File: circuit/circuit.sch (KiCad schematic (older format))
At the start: 19 parts

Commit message: circuit building
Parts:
- added BATT1, BATT2, BATT3, BATT4: M02PTH, SparkFun:SparkFun-1X02_XTRA_BIG, symbol M02PTH
- added C-ADC1: 100n, Capacitors_SMD:C_0805_HandSoldering, symbol C
- added CON-PV1: BARREL_JACK, Connect:JACK_ALIM, symbol BARREL_JACK
- added C_VUSB1, C_VUSB2: 100u, Capacitors_ThroughHole:C_Radial_D5_L6_P2.5, symbol CP
- added D-3V3, D-LAMP1, D-PV1, D-USB1, D-VDD1: D, Diodes_SMD:SMA_Handsoldering, symbol D
- added D-VUSB1, D-VUSB2: D_Schottky, Diodes_SMD:SMA_Handsoldering, symbol D_Schottky
- added D1: 5v1, Diodes_SMD:MELF_Handsoldering, symbol ZENER
- added IC-VUSB1: LM2596S, TO_SOT_Packages_SMD:TO-263-5Lead, symbol LM2596S
- added L-VUSB1: INDUCTOR, Inductors:INDUCTOR_V, symbol INDUCTOR
- added OK-LAMP1, OK-PV1, OK-PV2, OK-USB1: PC817, Housings_DIP:DIP-4_W7.62mm, symbol PC817
- added P-VDD-3V3, SW-PWR1: CONN_01X02, Pin_Headers:Pin_Header_Straight_1x02, symbol CONN_01X02
- added P1: USB_A, Connect:USB_A, symbol USB_A
- added R-ADC-BATT1: 470k, Resistors_ThroughHole:Resistor_Horizontal_RM10mm, symbol R
- added R-ADC-BATT2: 100k, Resistors_ThroughHole:Resistor_Horizontal_RM10mm, symbol R
- added R-LAMP1, R-PV3, R-USB1: 330, Resistors_SMD:R_0805_HandSoldering, symbol R
- added R-LAMP2, R-PV1, R-PV4, R-USB2: 4k7, Resistors_SMD:R_0805_HandSoldering, symbol R
- added R-PV2: 100k, Resistors_SMD:R_0805_HandSoldering, symbol R
- added TR-LAMP1, TR-USB1: IRF530_TO220BV, transistor-power:TO220BV, symbol IRF530_TO220BV
- added TR-PV1: IRF9530_TO220BV, transistor-power:TO220BV, symbol IRF9530_TO220BV
- added U1: MIC5219BM5_SOT23-5, TO_SOT_Packages_SMD:SOT-23-5, symbol MIC5219BM5_SOT23-5
- L-LAMP1, L-PV1, L-USB1, L1, L2, L3, L4: footprint LEDs:LED-1206 -> LEDs:LED-0805
- R-L-LAMP1, R-L-PV1, R-L-USB1, R-L1, R-L2, R-L3, R-L4, R-NRST1: footprint Resistors_SMD:R_1206_HandSoldering -> Resistors_SMD:R_0805_HandSoldering
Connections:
- net +3V3: now also D-3V3.1 (K), P-VDD-3V3.2 (P2)
- net ADC_BATT: now also C-ADC1.1, R-ADC-BATT1.2, R-ADC-BATT2.1
- net ADC_USB: now also D-VUSB2.2 (A), P1.4 (GND), P1.5 (shield)
- net GND: now also C-ADC1.2, C_VUSB1.2, C_VUSB2.2, D-VUSB1.2 (A), D-VUSB2.1 (K), D1.2 (A), IC-VUSB1.3 (GND), IC-VUSB1.5 (EN), IC-VUSB1.6 (GND@1), OK-LAMP1.2, OK-PV1.2, OK-PV2.2, OK-USB1.2, R-ADC-BATT2.2, R-LAMP2.2, R-PV1.2, R-USB2.2, SW-PWR1.1 (P1), U1.2 (GND)
- net RX: now also P-COMM1.3 (P3); no longer P-COMM1.4 (P4)
- net TX: now also P-COMM1.4 (P4); no longer P-COMM1.3 (P3)
- net VDD: now also D-VDD1.1 (K), OK-PV1.4, P-VDD-3V3.1 (P1)
- net CON_PV: now reaches STM32.25 (PB12/TIM1_BKIN)
- net CON_PV: now also R-PV3.1
- net CON_LAMP: now reaches STM32.26 (PB13/TIM1_CH1N)
- net CON_LAMP: now also R-LAMP1.1
- net CON_USB: now reaches STM32.27 (PB14/TIM1_CH2N)
- net CON_USB: now also R-USB1.1
- net ADC_PV_WKUP renamed IND_PV_WKUP
- net IND_PV_WKUP: now also OK-PV1.3, R-PV1.1
- new net: BATT1.1, BATT2.2
- new net: BATT3.1, BATT4.2, D-VDD1.2 (A)
- new net: OK-PV1.1, R-PV2.2
- new net: D-3V3.2 (A), U1.5 (OUT)
- new net: OK-PV2.1, R-PV3.2
- new net: OK-PV2.3, R-PV4.1, TR-PV1.G
- new net: D-PV1.2 (A), TR-PV1.D
- new net: OK-LAMP1.1, R-LAMP1.2
- new net: OK-LAMP1.3, R-LAMP2.1, TR-LAMP1.G
- new net: D-LAMP1.1 (K), OK-LAMP1.4, TR-LAMP1.D
- new net: C_VUSB1.1, IC-VUSB1.1 (IN), TR-USB1.S
- new net: D-VUSB1.1 (K), IC-VUSB1.2 (OUT), L-VUSB1.2
- new net: C_VUSB2.1, D1.1 (K), IC-VUSB1.4 (FB), L-VUSB1.1, P1.1 (VCC)
- new net: OK-USB1.1, R-USB1.2
- new net: OK-USB1.3, R-USB2.1, TR-USB1.G
- new net: D-USB1.1 (K), OK-USB1.4, TR-USB1.D
- new net +15V: BATT1.2, D-LAMP1.2 (A), D-PV1.1 (K), D-USB1.2 (A), R-ADC-BATT1.1
- new net +24V: CON-PV1.1, OK-PV2.4, R-PV2.1, TR-PV1.S
- new net +6V: BATT2.1, BATT3.2, U1.1 (IN), U1.3 (EN)
- new net GNDPWR: BATT4.1, CON-PV1.2, CON-PV1.3, R-PV4.2, SW-PWR1.2 (P2)
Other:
- moved on the sheet: L-LAMP1, L-PV1, L-USB1, L1, L2, L3, L4, P-BOOT1, P-COMM1, R-L-LAMP1, R-L-PV1, R-L-USB1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

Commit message: development
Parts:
- added L-IND1: LED, LEDs:LED-0805, symbol LED
- added R-L-IND1: 330, Resistors_SMD:R_0805_HandSoldering, symbol R
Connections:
- net GND: now also L-IND1.1 (K)
- net L-IND: now reaches STM32.38 (JTDI/PA15)
- net L-IND: now also R-L-IND1.2
- new net: L-IND1.2 (A), R-L-IND1.1
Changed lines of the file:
@@
 $EndComp
 $Comp
-L GND #PWR30
+L GND #PWR31
 U 1 1 572719C0
 P 10350 3550
-F 0 "#PWR30" H 10350 3300 50  0001 C CNN
+F 0 "#PWR31" H 10350 3300 50  0001 C CNN
 F 1 "GND" H 10350 3400 50  0000 C CNN
 F 2 "" H 10350 3550 50  0000 C CNN
@@
 $EndComp
 $Comp
-L VDD #PWR28
+L VDD #PWR29
 U 1 1 572734AE
 P 9750 3150
-F 0 "#PWR28" H 9750 3000 50  0001 C CNN
+F 0 "#PWR29" H 9750 3000 50  0001 C CNN
 F 1 "VDD" H 9750 3300 50  0000 C CNN
 F 2 "" H 9750 3150 50  0000 C CNN
@@
 $EndComp
 $Comp
-L GND #PWR24
+L GND #PWR25
 U 1 1 572742F8
 P 9650 3850
-F 0 "#PWR24" H 9650 3600 50  0001 C CNN
+F 0 "#PWR25" H 9650 3600 50  0001 C CNN
 F 1 "GND" H 9650 3700 50  0000 C CNN
 F 2 "" H 9650 3850 50  0000 C CNN
@@
 IND_PV_WKUP
 $Comp
-L GNDPWR #PWR34
+L GNDPWR #PWR35
 U 1 1 57276075
 P 10700 2900
-F 0 "#PWR34" H 10700 2700 50  0001 C CNN
+F 0 "#PWR35" H 10700 2700 50  0001 C CNN
 F 1 "GNDPWR" H 10700 2770 50  0000 C CNN
 F 2 "" H 10700 2850 50  0000 C CNN
@@
 $EndComp
 $Comp
-L +24V #PWR29
+L +24V #PWR30
 U 1 1 572762B3
 P 10200 2850
-F 0 "#PWR29" H 10200 2700 50  0001 C CNN
+F 0 "#PWR30" H 10200 2700 50  0001 C CNN
 F 1 "+24V" H 10200 2990 50  0000 C CNN
 F 2 "" H 10200 2850 50  0000 C CNN
@@
 $EndComp
 $Comp
-L +24V #PWR36
+L +24V #PWR37
 U 1 1 5727D109
 P 10800 4250
-F 0 "#PWR36" H 10800 4100 50  0001 C CNN
+F 0 "#PWR37" H 10800 4100 50  0001 C CNN
 F 1 "+24V" H 10800 4390 50  0000 C CNN
 F 2 "" H 10800 4250 50  0000 C CNN
@@
 $EndComp
 $Comp
-L GND #PWR25
+L GND #PWR26
 U 1 1 5727D72F
 P 9650 4700
-F 0 "#PWR25" H 9650 4450 50  0001 C CNN
+F 0 "#PWR26" H 9650 4450 50  0001 C CNN
 F 1 "GND" H 9650 4550 50  0000 C CNN
 F 2 "" H 9650 4700 50  0000 C CNN
@@
 $EndComp
 $Comp
-L GNDPWR #PWR31
+L GNDPWR #PWR32
 U 1 1 5727E52D
 P 10450 5100
-F 0 "#PWR31" H 10450 4900 50  0001 C CNN
+F 0 "#PWR32" H 10450 4900 50  0001 C CNN
 F 1 "GNDPWR" H 10450 4970 50  0000 C CNN
 F 2 "" H 10450 5050 50  0000 C CNN
@@
 $EndComp
 $Comp
-L +15V #PWR38
+L +15V #PWR39
 U 1 1 5727EAFC
 P 11100 4800
-F 0 "#PWR38" H 11100 4650 50  0001 C CNN
+F 0 "#PWR39" H 11100 4650 50  0001 C CNN
 F 1 "+15V" H 11100 4940 50  0000 C CNN
 F 2 "" H 11100 4800 50  0000 C CNN
@@
 $EndComp
 $Comp
-L +15V #PWR37
+L +15V #PWR38
 U 1 1 57283181
 P 10850 5400
-F 0 "#PWR37" H 10850 5250 50  0001 C CNN
+F 0 "#PWR38" H 10850 5250 50  0001 C CNN
 F 1 "+15V" H 10850 5540 50  0000 C CNN
 F 2 "" H 10850 5400 50  0000 C CNN
@@
 $EndComp
 $Comp
-L GND #PWR26
+L GND #PWR27
 U 1 1 57283C11
 P 9650 6200
-F 0 "#PWR26" H 9650 5950 50  0001 C CNN
+F 0 "#PWR27" H 9650 5950 50  0001 C CNN
 F 1 "GND" H 9650 6050 50  0000 C CNN
 F 2 "" H 9650 6200 50  0000 C CNN
@@
 Connection ~ 10500 6200
 $Comp
-L GND #PWR33
+L GND #PWR34
 U 1 1 57289B95
 P 10500 6600
-F 0 "#PWR33" H 10500 6350 50  0001 C CNN
+F 0 "#PWR34" H 10500 6350 50  0001 C CNN
 F 1 "GND" H 10500 6450 50  0000 C CNN
 F 2 "" H 10500 6600 50  0000 C CNN
@@
 Connection ~ 10750 7550
 $Comp
-L +15V #PWR35
+L +15V #PWR36
 U 1 1 5728C61B
 P 10750 7000
-F 0 "#PWR35" H 10750 6850 50  0001 C CNN
+F 0 "#PWR36" H 10750 6850 50  0001 C CNN
 F 1 "+15V" H 10750 7140 50  0000 C CNN
 F 2 "" H 10750 7000 50  0000 C CNN
@@
 	10750 7000 10750 7150
 $Comp
-L GND #PWR27
+L GND #PWR28
 U 1 1 5728DC8C
 P 9650 7950
-F 0 "#PWR27" H 9650 7700 50  0001 C CNN
+F 0 "#PWR28" H 9650 7700 50  0001 C CNN
 F 1 "GND" H 9650 7800 50  0000 C CNN
 F 2 "" H 9650 7950 50  0000 C CNN
@@
 	9650 7900 9650 7950
 $Comp
-L GND #PWR32
+L GND #PWR33
 U 1 1 5728F192
 P 10450 8350
-F 0 "#PWR32" H 10450 8100 50  0001 C CNN
+F 0 "#PWR33" H 10450 8100 50  0001 C CNN
 F 1 "GND" H 10450 8200 50  0000 C CNN
 F 2 "" H 10450 8350 50  0000 C CNN
@@
 U 1 1 57274EE9
 P 6700 8250
-F 0 "U1" H 6700 8250 0   0001 C CNN
-F 1 "MIC5219BM5_SOT23-5" H 6700 8250 0   0001 C CNN
+F 0 "U1" H 6700 8250 60  0001 C CNN
+F 1 "MIC5219BM5_SOT23-5" H 6700 8250 60  0001 C CNN
 F 2 "TO_SOT_Packages_SMD:SOT-23-5" H 6700 8250 60  0001 C CNN
 F 3 "" H 6700 8250 60  0000 C CNN
@@
 	10950 8200 10750 8200
 $Comp
-L GND #PWR39
+L GND #PWR40
 U 1 1 57283CF9
 P 11200 8700
-F 0 "#PWR39" H 11200 8450 50  0001 C CNN
+F 0 "#PWR40" H 11200 8450 50  0001 C CNN
 F 1 "GND" H 11200 8550 50  0000 C CNN
 F 2 "" H 11200 8700 50  0000 C CNN
@@
 Wire Wire Line
 	10750 8200 10750 8000
+Wire Wire Line
+	6900 4500 7150 4500
+Text Label 7150 4500 0    60   ~ 0
+L-IND
+$Comp
+L R R-L-IND1
+U 1 1 57284423
+P 8300 6350
+F 0 "R-L-IND1" V 8380 6350 50  0000 C CNN
+F 1 "330" V 8300 6350 50  0000 C CNN
+F 2 "Resistors_SMD:R_0805_HandSoldering" V 8230 6350 50  0001 C CNN
+F 3 "" H 8300 6350 50  0000 C CNN
+	1    8300 6350
+	0    1    1    0
+$EndComp
+$Comp
+L LED L-IND1
+U 1 1 57284429
+P 8750 6350
+F 0 "L-IND1" H 8750 6450 50  0000 C CNN
+F 1 "LED" H 8750 6250 50  0000 C CNN
+F 2 "LEDs:LED-0805" H 8750 6350 50  0001 C CNN
+F 3 "" H 8750 6350 50  0000 C CNN
+	1    8750 6350
+	-1   0    0    1
+$EndComp
+Text Label 8050 6350 0    60   ~ 0
+L-IND
+$Comp
+L GND #PWR24
+U 1 1 57284430
+P 8950 6450
+F 0 "#PWR24" H 8950 6200 50  0001 C CNN
+F 1 "GND" H 8950 6300 50  0000 C CNN
+F 2 "" H 8950 6450 50  0000 C CNN
+F 3 "" H 8950 6450 50  0000 C CNN
+	1    8950 6450
+	1    0    0    -1
+$EndComp
+Wire Wire Line
+	8550 6350 8450 6350
+Wire Wire Line
+	8150 6350 8050 6350
+Wire Wire Line
+	8950 6350 8950 6450
 $EndSCHEMATC

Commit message: circuit building
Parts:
- added C-VREG1, C-VREG2: C, Capacitors_SMD:C_0805_HandSoldering, symbol C
- added D-LAMP2: D, Diodes_SMD:SMA_Handsoldering, symbol D
- added D-LAMP3: D_Schottky, Diodes_SMD:SMA_Handsoldering, symbol D_Schottky
- added J1: audio-jack, audio-lamp:JACK_LAPAN, symbol audio-jack
- added P2: CONN_01X04, Pin_Headers:Pin_Header_Straight_1x04, symbol CONN_01X04
- added PIN1: CONN_01X03, Pin_Headers:Pin_Header_Straight_1x03, symbol CONN_01X03
- added PIN2: CONN_01X06, Pin_Headers:Pin_Header_Straight_1x06, symbol CONN_01X06
- added PIN3: CONN_01X02, Pin_Headers:Pin_Header_Straight_1x02, symbol CONN_01X02
- U1: symbol MIC5219BM5_SOT23-5 -> MIC5219BM5_SOT23-5-RESCUE-circuit
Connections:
- net ADC_LAMP: now also D-LAMP3.2 (A), J1.1 (V-)
- net BOOT0: now also P-BOOT1.2 (P2); no longer P-BOOT1.1 (P1)
- net GND: now also C-VREG1.2, C-VREG2.2, D-LAMP3.1 (K)
- net VDD: now also P-BOOT1.1 (P1), STM32.1 (VBAT); no longer P-BOOT1.2 (P2)
- net AIN4: now reaches STM32.14 (SPI1_NSS/ADC1_IN4/USART2_CK/DAC1_OUT/PA4)
- net AIN4: now also PIN2.1 (P1)
- net AIN5: now reaches STM32.15 (SPI1_SCK/ADC1_IN5/DAC2_OUT/PA5)
- net AIN5: now also PIN2.2 (P2)
- net AIN6: now reaches STM32.16 (SPI1_MISO/ADC1_IN6/TIM3_CH1/PA6)
- net AIN6: now also PIN2.3 (P3)
- net AIN7: now reaches STM32.17 (SPI1_MOSI/ADC1_IN7/TIM3_CH2/PA7)
- net AIN7: now also PIN2.4 (P4)
- net AIN8: now reaches STM32.18 (PB0/ADC1_IN8/TIM3_CH3)
- net AIN8: now also PIN2.5 (P5)
- net AIN9: now reaches STM32.19 (PB1/ADC1_IN9/TIM3_CH4)
- net AIN9: now also PIN2.6 (P6)
- net PC13: now reaches STM32.2 (PC13/TAMPER_RTC)
- net PC13: now also PIN1.1 (P1)
- net PB15: now reaches STM32.28 (PB15/TIM1_CH3N/TIM15_CH1N)
- net PB15: now also PIN3.1 (P1)
- net PA8: now reaches STM32.29 (USART1_CK/MCO/TIM1_CH1/PA8)
- net PA8: now also PIN3.2 (P2)
- net PC14: now reaches STM32.3 (PC14/OSC32_IN)
- net PC14: now also PIN1.2 (P2)
- net PA11: now reaches STM32.32 (USART1_CTS/TIM1_CH4/PA11)
- net PA11: now also P2.1 (P1)
- net PA12: now reaches STM32.33 (USART1_RTS/TIM1_ETR/PA12)
- net PA12: now also P2.2 (P2)
- net PA13: now reaches STM32.34 (JTMS/SWDIO/PA13)
- net PA13: now also P2.3 (P3)
- net PA14: now reaches STM32.37 (JTCK/SWCLK/PA14)
- net PA14: now also P2.4 (P4)
- net PC15: now reaches STM32.4 (PC15/OSC32_OUT)
- net PC15: now also PIN1.3 (P3)
- net at U1.4 (BYP): now also C-VREG1.1
- net at D-3V3.2 (A), U1.5 (OUT): now also C-VREG2.1
- net at TR-LAMP1.S: now also D-LAMP2.2 (A)
- new net: D-LAMP2.1 (K), J1.2 (V+)

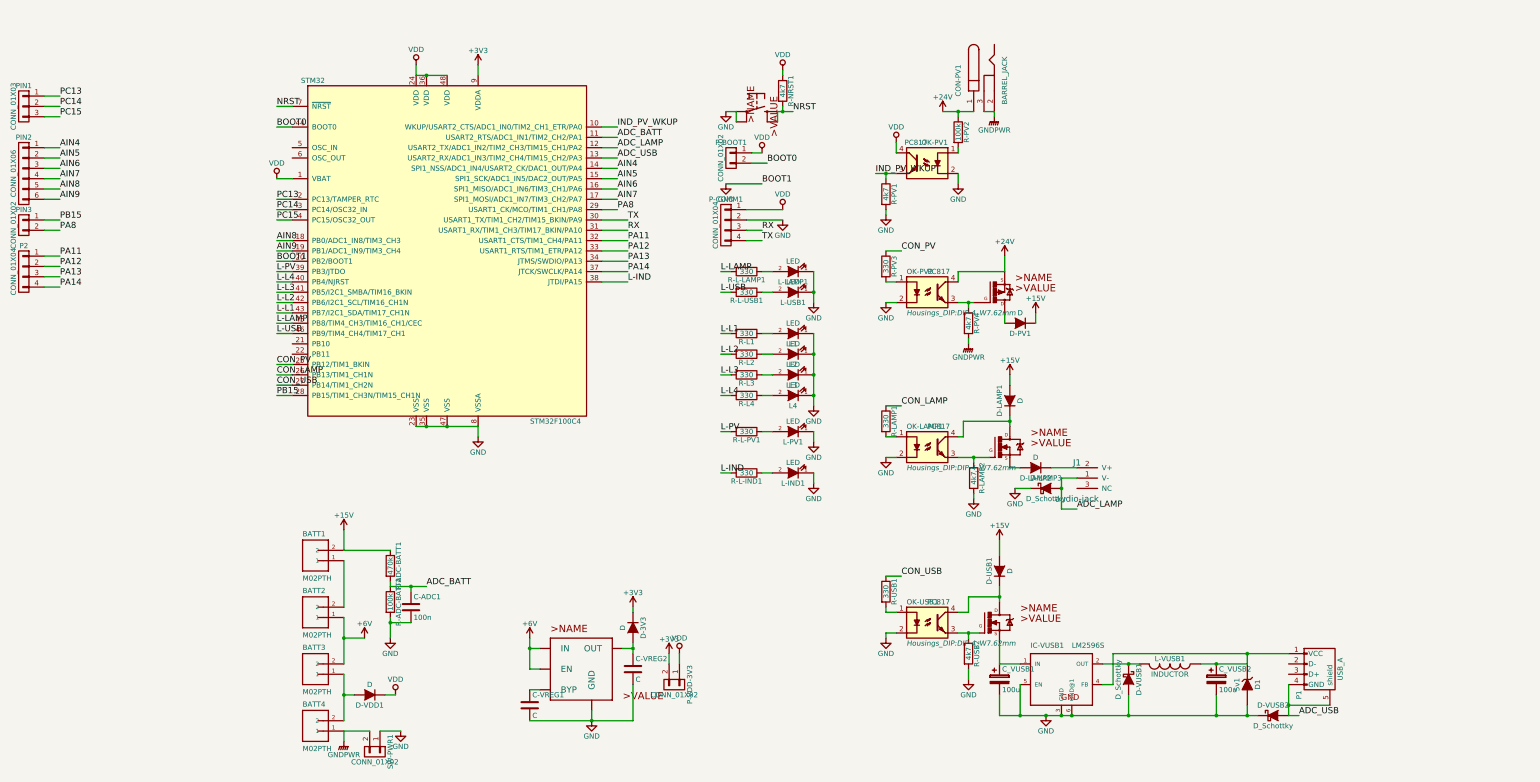
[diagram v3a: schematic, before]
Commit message: tambah test pad
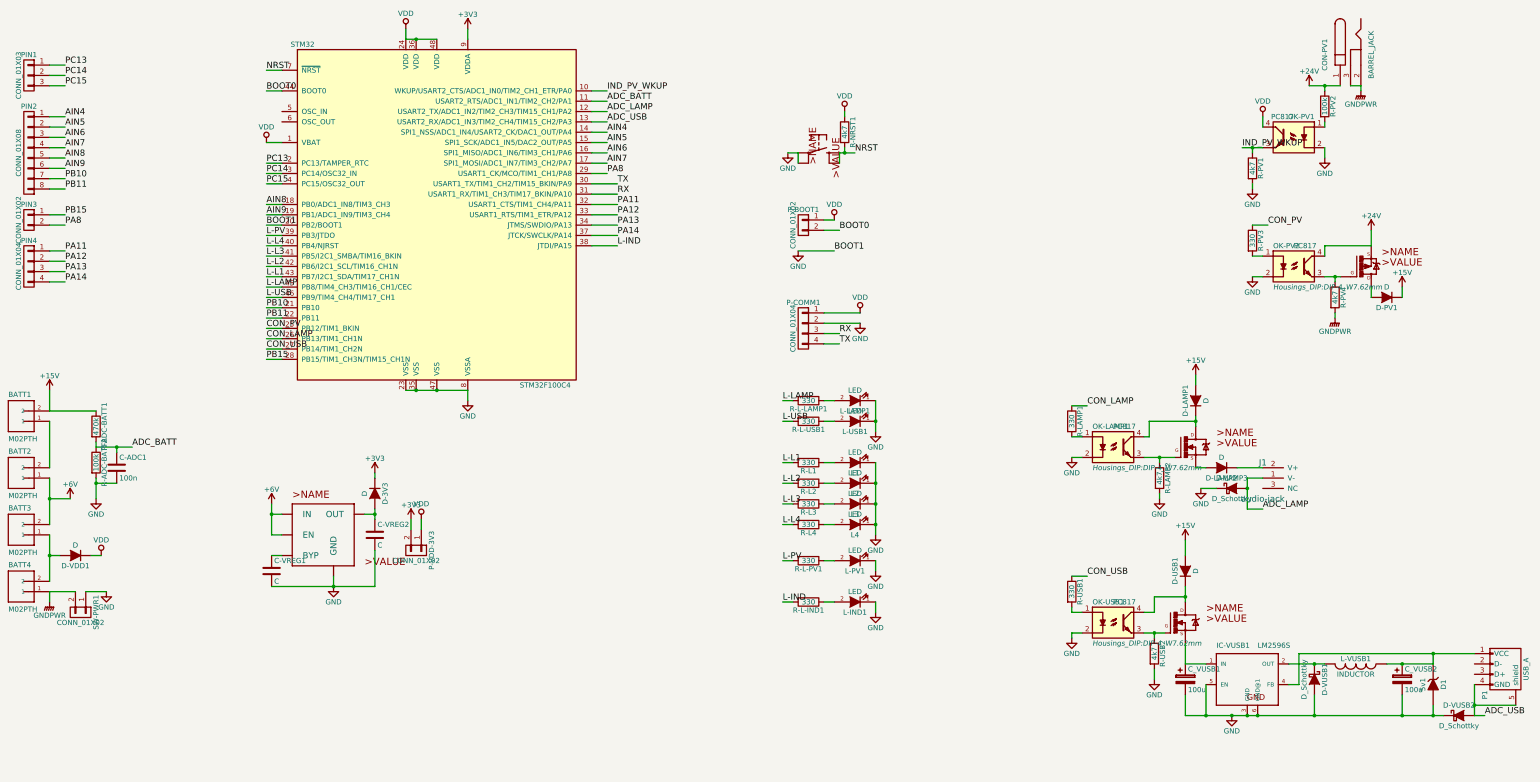
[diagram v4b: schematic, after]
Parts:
- removed PIN2: CONN_01X06, Pin_Headers:Pin_Header_Straight_1x06, symbol CONN_01X06
- added PIN2: CONN_01X08, Pin_Headers:Pin_Header_Straight_1x08, symbol CONN_01X08
- renumbered P2 to PIN4
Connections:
- net AIN4: now also PIN2.1 (P1)
- net AIN5: now also PIN2.2 (P2)
- net AIN6: now also PIN2.3 (P3)
- net AIN7: now also PIN2.4 (P4)
- net AIN8: now also PIN2.5 (P5)
- net AIN9: now also PIN2.6 (P6)
- net PB10: now reaches STM32.21 (PB10)
- net PB10: now also PIN2.7 (P7)
- net PB11: now reaches STM32.22 (PB11)
- net PB11: now also PIN2.8 (P8)
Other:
- moved on the sheet: BATT1, BATT2, BATT3, BATT4, C-ADC1, C-VREG1, C-VREG2, CON-PV1, C_VUSB1, C_VUSB2, D-3V3, D-LAMP1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
